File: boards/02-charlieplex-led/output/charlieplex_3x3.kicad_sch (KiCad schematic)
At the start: 14 parts, among them U1 MCU

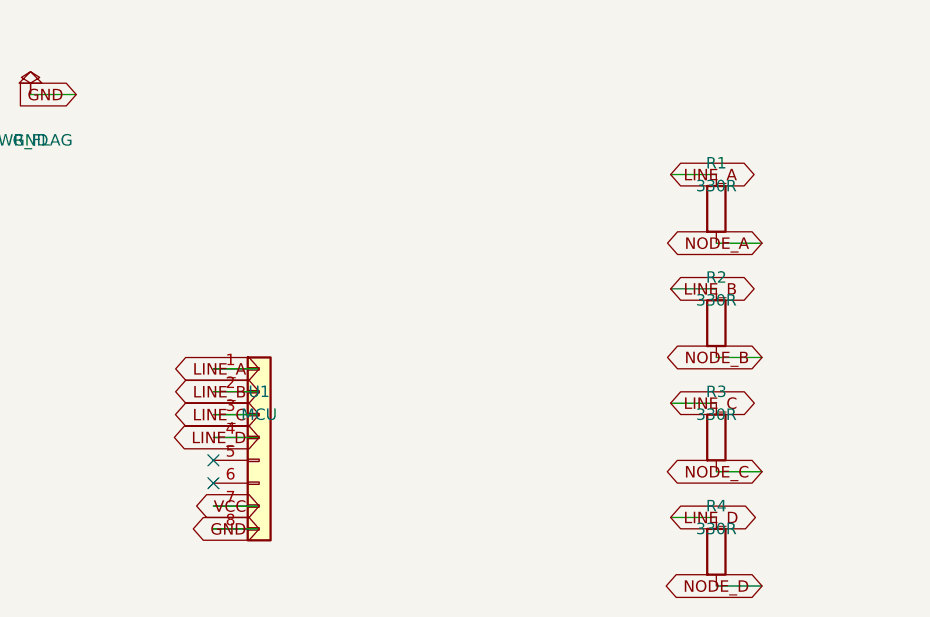
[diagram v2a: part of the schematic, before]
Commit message: fix(footprint): use R_0805 in default profile and fix board 02 U1 footprint (#1545)
Change the default footprint selector profile to map all resistor values
to R_0805_2012Metric instead of R_0402_1005Metric, matching what the PCB
generation scripts actually place. Also fix board 02's U1 schematic
footprint from PinHeader_1x08 to DIP-8_W7.62mm to match its PCB footprint.

Regenerate output files for boards 01 and 02 to reflect corrected footprints.

Co-authored-by: Claude Opus 4.6 <noreply@anthropic.com>
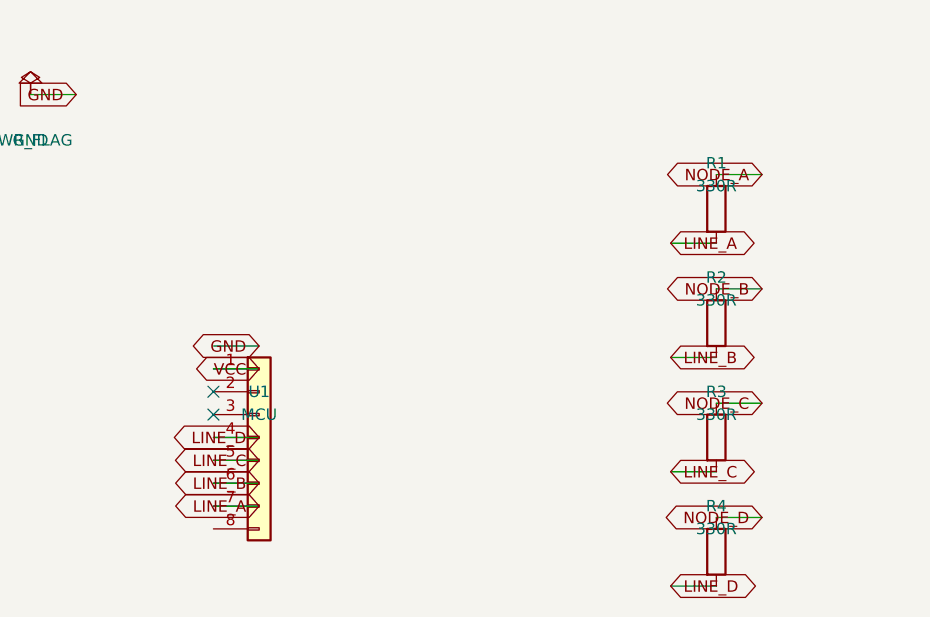
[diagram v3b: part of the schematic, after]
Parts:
- R1, R2, R3, R4: footprint Resistor_SMD:R_0402_1005Metric -> Resistor_SMD:R_0805_2012Metric
- U1: footprint Connector_PinHeader_2.54mm:PinHeader_1x08_P2.54mm_Vertical -> Package_DIP:DIP-8_W7.62mm
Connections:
- net GND: no longer U1.8 (Pin_8)
- net LINE_A: now also R1.2, U1.7 (Pin_7); no longer R1.1, U1.1 (Pin_1)
- net LINE_B: now also R2.2, U1.6 (Pin_6); no longer R2.1, U1.2 (Pin_2)
- net LINE_C: now also R3.2, U1.5 (Pin_5); no longer R3.1, U1.3 (Pin_3)
- net LINE_D: now also R4.2; no longer R4.1
- net NODE_A: now also R1.1; no longer R1.2
- net NODE_B: now also R2.1; no longer R2.2
- net NODE_C: now also R3.1; no longer R3.2
- net NODE_D: now also R4.1; no longer R4.2
- net VCC: now also U1.1 (Pin_1); no longer U1.7 (Pin_7)

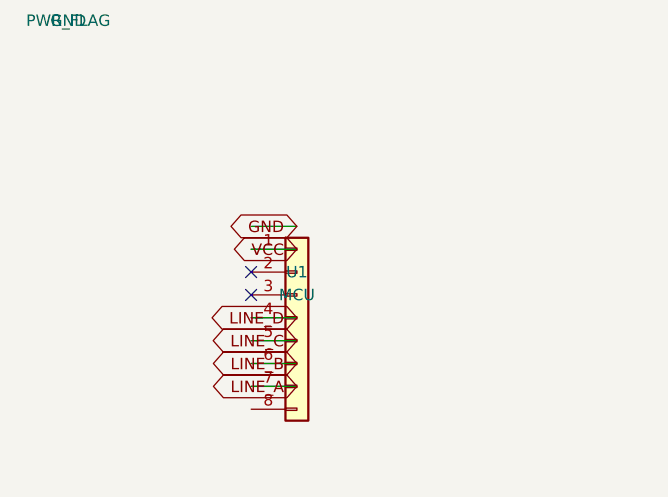
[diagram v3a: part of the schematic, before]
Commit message: fix(boards): connect unused MCU pins to GND in boards 02 and 03
Unused MCU digital input pins were left without net assignments in the
PCB generators, producing pads with no net clause in the KiCad PCB
files. JLCPCB's automated review flags these unconnected pads and holds
orders for clarification. Connect all unused inputs to GND -- standard
practice that prevents floating inputs and eliminates review holds.

Board 02: pins 5, 6 (GND net 10)
Board 03: pins 5, 6, 18, 19, 20, 21, 22, 31 (GND net 3)

Co-Authored-By: Claude Opus 4.6 <noreply@anthropic.com>
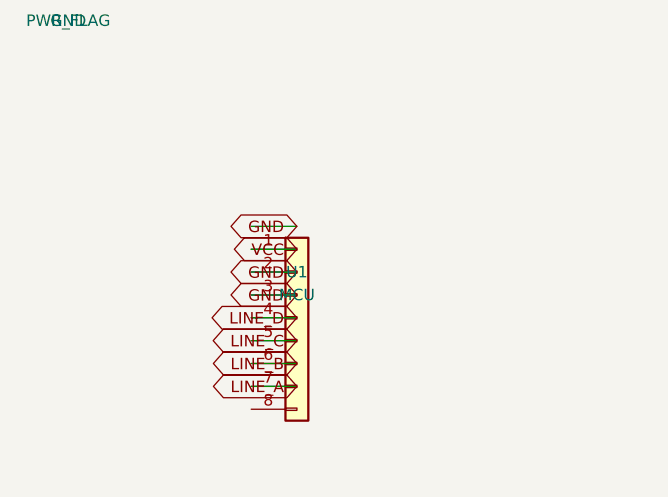
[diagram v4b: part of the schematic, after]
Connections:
- net GND: now also U1.2 (Pin_2), U1.3 (Pin_3)
- no-connect marks 2 -> 0
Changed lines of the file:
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@@
     (instances
       (project "project"
-        (path "/5f8dae7f-3341-4b1b-add0-f1d1c611d5f4" (reference "U1") (unit 1)
+        (path "/7f2392ee-fbec-4c48-8445-d1a68583055f" (reference "U1") (unit 1)
         )
       )
@@
     (instances
       (project "project"
-        (path "/5f8dae7f-3341-4b1b-add0-f1d1c611d5f4" (reference "R1") (unit 1)
+        (path "/7f2392ee-fbec-4c48-8445-d1a68583055f" (reference "R1") (unit 1)
         )
       )
@@
     (instances
       (project "project"
-        (path "/5f8dae7f-3341-4b1b-add0-f1d1c611d5f4" (reference "R2") (unit 1)
+        (path "/7f2392ee-fbec-4c48-8445-d1a68583055f" (reference "R2") (unit 1)
         )
       )
@@
     (instances
       (project "project"
-        (path "/5f8dae7f-3341-4b1b-add0-f1d1c611d5f4" (reference "R3") (unit 1)
+        (path "/7f2392ee-fbec-4c48-8445-d1a68583055f" (reference "R3") (unit 1)
         )
       )
@@
     (instances
       (project "project"
-        (path "/5f8dae7f-3341-4b1b-add0-f1d1c611d5f4" (reference "R4") (unit 1)
+        (path "/7f2392ee-fbec-4c48-8445-d1a68583055f" (reference "R4") (unit 1)
         )
       )
@@
     (instances
       (project "project"
-        (path "/5f8dae7f-3341-4b1b-add0-f1d1c611d5f4" (reference "D1") (unit 1)
+        (path "/7f2392ee-fbec-4c48-8445-d1a68583055f" (reference "D1") (unit 1)
         )
       )
@@
     (instances
       (project "project"
-        (path "/5f8dae7f-3341-4b1b-add0-f1d1c611d5f4" (reference "D2") (unit 1)
+        (path "/7f2392ee-fbec-4c48-8445-d1a68583055f" (reference "D2") (unit 1)
         )
       )
@@
     (instances
       (project "project"
-        (path "/5f8dae7f-3341-4b1b-add0-f1d1c611d5f4" (reference "D3") (unit 1)
+        (path "/7f2392ee-fbec-4c48-8445-d1a68583055f" (reference "D3") (unit 1)
         )
       )
@@
     (instances
       (project "project"
-        (path "/5f8dae7f-3341-4b1b-add0-f1d1c611d5f4" (reference "D4") (unit 1)
+        (path "/7f2392ee-fbec-4c48-8445-d1a68583055f" (reference "D4") (unit 1)
         )
       )
@@
     (instances
       (project "project"
-        (path "/5f8dae7f-3341-4b1b-add0-f1d1c611d5f4" (reference "D5") (unit 1)
+        (path "/7f2392ee-fbec-4c48-8445-d1a68583055f" (reference "D5") (unit 1)
         )
       )
@@
     (instances
       (project "project"
-        (path "/5f8dae7f-3341-4b1b-add0-f1d1c611d5f4" (reference "D6") (unit 1)
+        (path "/7f2392ee-fbec-4c48-8445-d1a68583055f" (reference "D6") (unit 1)
         )
       )
@@
     (instances
       (project "project"
-        (path "/5f8dae7f-3341-4b1b-add0-f1d1c611d5f4" (reference "D7") (unit 1)
+        (path "/7f2392ee-fbec-4c48-8445-d1a68583055f" (reference "D7") (unit 1)
         )
       )
@@
     (instances
       (project "project"
-        (path "/5f8dae7f-3341-4b1b-add0-f1d1c611d5f4" (reference "D8") (unit 1)
+        (path "/7f2392ee-fbec-4c48-8445-d1a68583055f" (reference "D8") (unit 1)
         )
       )
@@
     (instances
       (project "project"
-        (path "/5f8dae7f-3341-4b1b-add0-f1d1c611d5f4" (reference "D9") (unit 1)
+        (path "/7f2392ee-fbec-4c48-8445-d1a68583055f" (reference "D9") (unit 1)
         )
       )
@@
     (instances
       (project "project"
-        (path "/5f8dae7f-3341-4b1b-add0-f1d1c611d5f4" (reference "#PWR01") (unit 1)
+        (path "/7f2392ee-fbec-4c48-8445-d1a68583055f" (reference "#PWR01") (unit 1)
         )
       )
@@
     (instances
       (project "project"
-        (path "/5f8dae7f-3341-4b1b-add0-f1d1c611d5f4" (reference "#PWR02") (unit 1)
+        (path "/7f2392ee-fbec-4c48-8445-d1a68583055f" (reference "#PWR02") (unit 1)
         )
       )
@@
     (instances
       (project "project"
-        (path "/5f8dae7f-3341-4b1b-add0-f1d1c611d5f4" (reference "#PWR03") (unit 1)
+        (path "/7f2392ee-fbec-4c48-8445-d1a68583055f" (reference "#PWR03") (unit 1)
         )
       )
@@
     (instances
       (project "project"
-        (path "/5f8dae7f-3341-4b1b-add0-f1d1c611d5f4" (reference "#PWR04") (unit 1)
+        (path "/7f2392ee-fbec-4c48-8445-d1a68583055f" (reference "#PWR04") (unit 1)
         )
       )
@@
   )
   (wire
+    (pts (xy 45.72 86.36) (xy 50.8 86.36))
+    (stroke
+      (width 0)
+      (type default)
+    )
+  )
+  (wire
+    (pts (xy 45.72 83.82) (xy 50.8 83.82))
+    (stroke
+      (width 0)
+      (type default)
+    )
+  )
+  (wire
     (pts (xy 45.72 81.28) (xy 50.8 81.28))
     (stroke
@@
     )
   )
-  (no_connect (at 45.72 86.36)
-  )
-  (no_connect (at 45.72 83.82)
-  )
   (global_label "LINE_A" (shape bidirectional) (at 50.8 96.52 180) (fields_autoplaced yes)
     (effects
@@
     )
   )
+  (global_label "GND" (shape bidirectional) (at 50.8 86.36 180) (fields_autoplaced yes)
+    (effects
+      (font
+        (size 1.27 1.27)
+      )
+      (justify right)
+    )
+  )
+  (global_label "GND" (shape bidirectional) (at 50.8 83.82 180) (fields_autoplaced yes)
+    (effects
+      (font
+        (size 1.27 1.27)
+      )
+      (justify right)
+    )
+  )
   (global_label "VCC" (shape bidirectional) (at 50.8 81.28 180) (fields_autoplaced yes)
     (effects
@@
   )
   (sheet_instances
-    (path "/5f8dae7f-3341-4b1b-add0-f1d1c611d5f4" (page "1")
-    )
-  )
+    (path "/7f2392ee-fbec-4c48-8445-d1a68583055f" (page "1")
+    )
+  )
